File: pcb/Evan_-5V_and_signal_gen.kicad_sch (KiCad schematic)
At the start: 28 parts, among them IC1 TL7660IDGKR, IC2 TL081IDT, IC4 UA78M33CDCYG3, J2 M22-6003005, U5 TPS2069CDBVR_MOSFET

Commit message: fix +5v connection, make final via (#17)
* fix +5v connection, make final via

* connect mcu 3.3vreg to +5v_ext so it always has power
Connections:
- net MOSFET_OUTPUT is gone; now on net +5V: C42.1, IC1.8 (VCC), U5.1 (OUT)
- net +5V: no longer C25.1, C41.1, IC4.1 (INPUT), J2.26, U5.5 (IN)
- new net +5V_EXT: C25.1, C41.1, IC4.1 (INPUT), J2.26, U5.5 (IN)
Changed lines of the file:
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@@
   (junction (at 133.35 55.88) (diameter 0) (color 0 0 0 0)
   )
+  (junction (at 207.01 86.868) (diameter 0) (color 0 0 0 0)
+  )
+  (junction (at 62.23 124.714) (diameter 0) (color 0 0 0 0)
+  )
   (junction (at 262.89 105.41) (diameter 0) (color 0 0 0 0)
   )
@@
   )
   (junction (at 156.21 27.94) (diameter 0) (color 0 0 0 0)
-  )
-  (junction (at 207.01 86.36) (diameter 0) (color 0 0 0 0)
   )
   (junction (at 104.14 38.1) (diameter 0) (color 0 0 0 0)
@@
     (stroke (width 0) (type default))
   )
+  (wire (pts (xy 62.23 124.46) (xy 140.462 124.46))
+    (stroke (width 0) (type default))
+  )
   (wire (pts (xy 77.47 96.52) (xy 77.47 95.25))
     (stroke (width 0) (type default))
@@
     (stroke (width 0) (type default))
   )
+  (wire (pts (xy 140.462 86.868) (xy 207.01 86.868))
+    (stroke (width 0) (type default))
+  )
   (wire (pts (xy 104.14 38.1) (xy 104.14 74.93))
     (stroke (width 0) (type default))
@@
     (stroke (width 0) (type default))
   )
+  (wire (pts (xy 29.718 83.82) (xy 29.718 124.714))
+    (stroke (width 0) (type default))
+  )
   (wire (pts (xy 44.45 158.75) (xy 44.45 161.29))
     (stroke (width 0) (type default))
   )
-  (wire (pts (xy 207.01 86.36) (xy 207.01 102.87))
+  (wire (pts (xy 207.01 86.36) (xy 207.01 86.868))
+    (stroke (width 0) (type default))
+  )
+  (wire (pts (xy 29.718 83.82) (xy 49.53 83.82))
     (stroke (width 0) (type default))
   )
@@
     (stroke (width 0) (type default))
   )
+  (wire (pts (xy 207.01 86.868) (xy 207.01 102.87))
+    (stroke (width 0) (type default))
+  )
   (wire (pts (xy 82.55 38.1) (xy 82.55 40.64))
     (stroke (width 0) (type default))
@@
     (stroke (width 0) (type default))
   )
+  (wire (pts (xy 62.23 124.714) (xy 29.718 124.714))
+    (stroke (width 0) (type default))
+  )
   (wire (pts (xy 95.25 33.02) (xy 95.25 35.56))
     (stroke (width 0) (type default))
@@
     (stroke (width 0) (type default))
   )
+  (wire (pts (xy 62.23 124.714) (xy 62.23 133.35))
+    (stroke (width 0) (type default))
+  )
   (wire (pts (xy 15.24 41.91) (xy 35.56 41.91))
     (stroke (width 0) (type default))
   )
+  (wire (pts (xy 140.462 124.46) (xy 140.462 86.868))
+    (stroke (width 0) (type default))
+  )
   (wire (pts (xy 262.89 78.74) (xy 262.89 91.44))
     (stroke (width 0) (type default))
@@
     (stroke (width 0) (type default))
   )
-  (wire (pts (xy 27.94 83.82) (xy 49.53 83.82))
-    (stroke (width 0) (type default))
-  )
   (wire (pts (xy 63.5 92.71) (xy 77.47 92.71))
     (stroke (width 0) (type default))
@@
     (stroke (width 0) (type default))
   )
-  (wire (pts (xy 207.01 85.09) (xy 207.01 86.36))
-    (stroke (width 0) (type default))
-  )
   (wire (pts (xy 157.48 39.37) (xy 165.1 39.37))
     (stroke (width 0) (type default))
@@
     (stroke (width 0) (type default))
   )
-  (wire (pts (xy 62.23 124.46) (xy 62.23 133.35))
+  (wire (pts (xy 62.23 124.46) (xy 62.23 124.714))
     (stroke (width 0) (type default))
   )
   (wire (pts (xy 262.89 119.38) (xy 262.89 123.19))
     (stroke (width 0) (type default))
+  )
+  (label "+5V_EXT" (at 164.084 86.868 0) (fields_autoplaced)
+    (effects (font (size 1.27 1.27)) (justify left bottom))
   )
   (global_label "ADC1_IN0_SINE" (shape input) (at 259.08 123.19 180) (fields_autoplaced)
@@
     )
   )
-  (global_label "MOSFET_OUTPUT" (shape input) (at 144.78 102.87 270) (fields_autoplaced)
-    (effects (font (size 1.27 1.27)) (justify right))
-    (property "Intersheetrefs" "${INTERSHEET_REFS}" (at 144.78 121.2161 90)
-      (effects (font (size 1.27 1.27)) (justify right) hide)
-    )
-  )
   (global_label "OBC_I2C_SDA" (shape input) (at 44.45 161.29 270) (fields_autoplaced)
     (effects (font (size 1.27 1.27)) (justify right))
@@
     (property "Intersheetrefs" "${INTERSHEET_REFS}" (at 52.07 177.9428 90)
       (effects (font (size 1.27 1.27)) (justify right) hide)
-    )
-  )
-  (global_label "MOSFET_OUTPUT" (shape input) (at 73.66 20.32 0) (fields_autoplaced)
-    (effects (font (size 1.27 1.27)) (justify left))
-    (property "Intersheetrefs" "${INTERSHEET_REFS}" (at 92.0061 20.32 0)
-      (effects (font (size 1.27 1.27)) (justify left) hide)
     )
   )
@@
     )
   )
+  (symbol (lib_id "power:+5V") (at 144.78 102.87 0) (unit 1)
+    (in_bom yes) (on_board yes) (dnp no)
+    (property "Reference" "#PWR09" (at 144.78 106.68 0)
+      (effects (font (size 1.27 1.27)) hide)
+    )
+    (property "Value" "+5V" (at 144.78 99.06 0)
+      (effects (font (size 1.27 1.27)))
+    )
+    (property "Footprint" "" (at 144.78 102.87 0)
+      (effects (font (size 1.27 1.27)) hide)
+    )
+    (property "Datasheet" "" (at 144.78 102.87 0)
+      (effects (font (size 1.27 1.27)) hide)
+    )
+    (pin "1")
+    (instances
+      (project "mcu_integration"
+        (path "/c0210bc3-f67f-47d8-a34e-f002a728adb2/39708197-8fe0-4b5c-ba49-65ed06982da9"
+          (reference "#PWR09") (unit 1)
+        )
+      )
+    )
+  )
   (symbol (lib_id "Device:R") (at 246.38 91.44 90) (unit 1)
     (in_bom yes) (on_board yes) (dnp no) (fields_autoplaced)
@@
     )
   )
-  (symbol (lib_id "power:+5V") (at 207.01 85.09 0) (unit 1)
-    (in_bom yes) (on_board yes) (dnp no)
-    (property "Reference" "#PWR09" (at 207.01 88.9 0)
-      (effects (font (size 1.27 1.27)) hide)
-    )
-    (property "Value" "+5V" (at 207.01 81.28 0)
-      (effects (font (size 1.27 1.27)))
-    )
-    (property "Footprint" "" (at 207.01 85.09 0)
-      (effects (font (size 1.27 1.27)) hide)
-    )
-    (property "Datasheet" "" (at 207.01 85.09 0)
-      (effects (font (size 1.27 1.27)) hide)
-    )
-    (pin "1")
-    (instances
-      (project "mcu_integration"
-        (path "/c0210bc3-f67f-47d8-a34e-f002a728adb2/39708197-8fe0-4b5c-ba49-65ed06982da9"
-          (reference "#PWR09") (unit 1)
+  (symbol (lib_id "power:+5V") (at 73.66 20.32 90) (unit 1)
+    (in_bom yes) (on_board yes) (dnp no) (fields_autoplaced)
+    (property "Reference" "#PWR016" (at 77.47 20.32 0)
+      (effects (font (size 1.27 1.27)) hide)
+    )
+    (property "Value" "+5V" (at 69.85 20.32 90)
+      (effects (font (size 1.27 1.27)) (justify left))
+    )
+    (property "Footprint" "" (at 73.66 20.32 0)
+      (effects (font (size 1.27 1.27)) hide)
+    )
+    (property "Datasheet" "" (at 73.66 20.32 0)
+      (effects (font (size 1.27 1.27)) hide)
+    )
+    (pin "1")
+    (instances
+      (project "mcu_integration"
+        (path "/c0210bc3-f67f-47d8-a34e-f002a728adb2/39708197-8fe0-4b5c-ba49-65ed06982da9"
+          (reference "#PWR016") (unit 1)
         )
       )
@@
         )
       )
-    )
-  )
-  (symbol (lib_id "power:+5V") (at 27.94 83.82 90) (unit 1)
-    (in_bom yes) (on_board yes) (dnp no) (fields_autoplaced)
-    (property "Reference" "#PWR035" (at 31.75 83.82 0)
-      (effects (font (size 1.27 1.27)) hide)
-    )
-    (property "Value" "+5V" (at 24.13 83.82 90)
-      (effects (font (size 1.27 1.27)) (justify left))
-    )
-    (property "Footprint" "" (at 27.94 83.82 0)
-      (effects (font (size 1.27 1.27)) hide)
-    )
-    (property "Datasheet" "" (at 27.94 83.82 0)
-      (effects (font (size 1.27 1.27)) hide)
-    )
-    (pin "1")
-    (instances
-      (project "mcu_integration"
-        (path "/c0210bc3-f67f-47d8-a34e-f002a728adb2/39708197-8fe0-4b5c-ba49-65ed06982da9"
-          (reference "#PWR035") (unit 1)
-        )
-      )
-    )
-  )
-  (symbol (lib_id "power:+5V") (at 62.23 124.46 0) (unit 1)
-    (in_bom yes) (on_board yes) (dnp no) (fields_autoplaced)
-    (property "Reference" "#PWR016" (at 62.23 128.27 0)
-      (effects (font (size 1.27 1.27)) hide)
-    )
-    (property "Value" "+5V" (at 62.23 119.38 0)
-      (effects (font (size 1.27 1.27)))
-    )
-    (property "Footprint" "" (at 62.23 124.46 0)
-      (effects (font (size 1.27 1.27)) hide)
-    )
-    (property "Datasheet" "" (at 62.23 124.46 0)
-      (effects (font (size 1.27 1.27)) hide)
-    )
-    (pin "1")
-    (instances
-      (project "mcu_integration"
-        (path "/c0210bc3-f67f-47d8-a34e-f002a728adb2/39708197-8fe0-4b5c-ba49-65ed06982da9"
-          (reference "#PWR016") (unit 1)
-        )
-      )

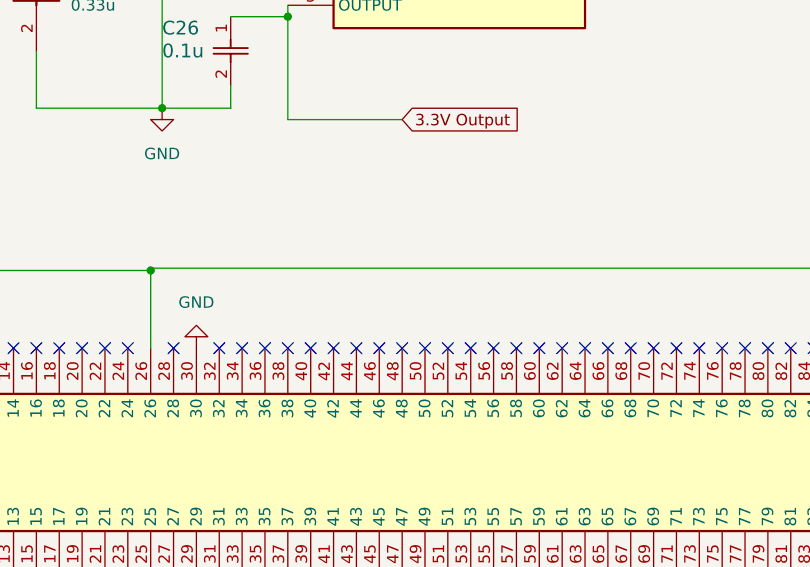
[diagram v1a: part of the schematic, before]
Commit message: TL766 footprint fixed
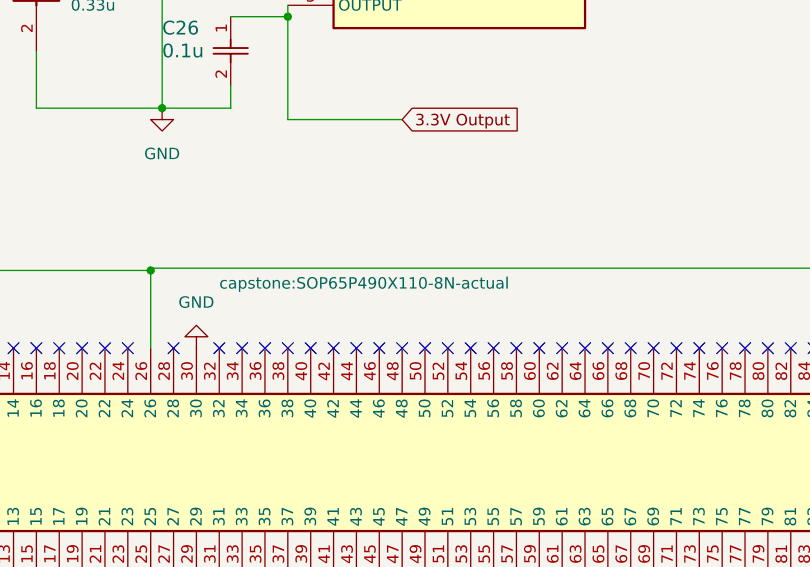
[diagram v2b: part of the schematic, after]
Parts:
- IC1: footprint capstone:SOIC127P600X175-8N -> capstone:SOP65P490X110-8N-actual
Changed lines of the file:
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@@
       (effects (font (size 1.27 1.27)))
     )
-    (property "Footprint" "capstone:SOIC127P600X175-8N" (at 69.85 125.4 0)
-      (effects (font (size 1.27 1.27)) (justify left top) hide)
+    (property "Footprint" "capstone:SOP65P490X110-8N-actual" (at 69.85 125.4 0)
+      (effects (font (size 1.27 1.27)) (justify left top))
     )
     (property "Datasheet" "http://www.ti.com/lit/gpn/tl7660" (at 69.85 225.4 0)

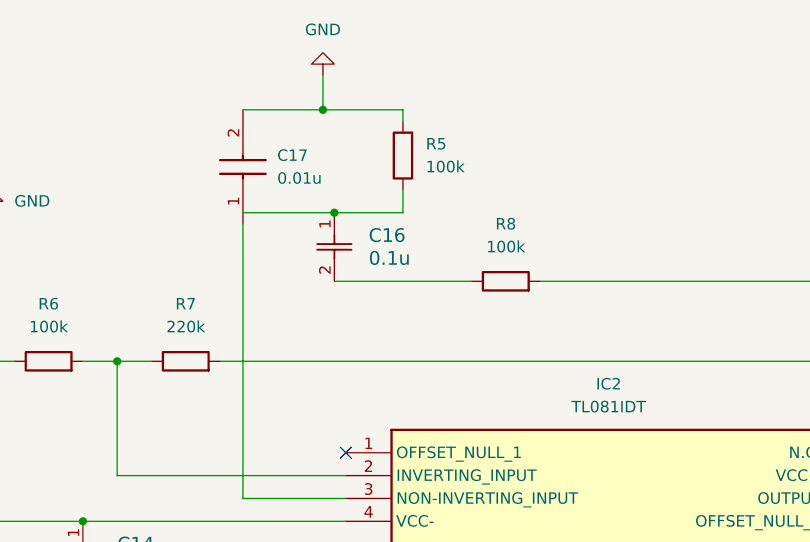
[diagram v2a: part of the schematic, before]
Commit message: hole sizing done, evan cap fix
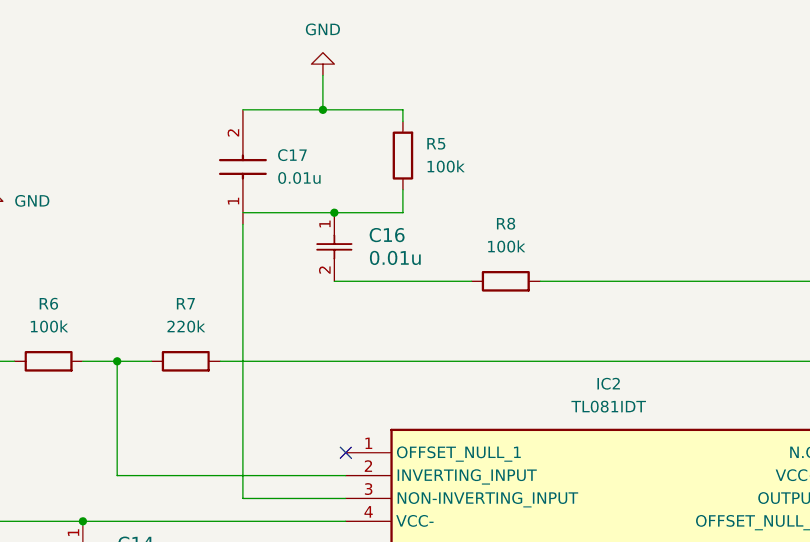
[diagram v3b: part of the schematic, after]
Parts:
- C16: value 0.1u -> 0.01u
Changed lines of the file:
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@@
       (effects (font (size 1.524 1.524)) (justify left))
     )
-    (property "Value" "0.1u" (at 161.29 44.45 90)
+    (property "Value" "0.01u" (at 161.29 44.45 90)
       (effects (font (size 1.524 1.524)) (justify left))
     )
